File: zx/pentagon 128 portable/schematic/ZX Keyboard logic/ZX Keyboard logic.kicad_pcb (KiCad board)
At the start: 2 copper layers, 99 x 66 mm, 51 parts, among them IC1 SN74LS245DW, IC2 SN74LS27N, IC3 SN74LS245DW, J1 Conn_01x03, J2 Conn_01x14, J3 Conn_01x02

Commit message: fixed keyboard
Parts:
- removed S1: 1, SamacSys_Parts:118259104
- removed S10: 0, SamacSys_Parts:118259104
- removed S11: Q, SamacSys_Parts:118259104
- removed S12: W, SamacSys_Parts:118259104
- removed S13: E, SamacSys_Parts:118259104
- removed S14: R, SamacSys_Parts:118259104
- removed S15: T, SamacSys_Parts:118259104
- removed S16: Y, SamacSys_Parts:118259104
- removed S17: U, SamacSys_Parts:118259104
- removed S18: I, SamacSys_Parts:118259104
- removed S19: O, SamacSys_Parts:118259104
- removed S2: 2, SamacSys_Parts:118259104
- removed S20: P, SamacSys_Parts:118259104
- removed S21: A, SamacSys_Parts:118259104
- removed S22: S, SamacSys_Parts:118259104
- removed S23: D, SamacSys_Parts:118259104
- removed S24: F, SamacSys_Parts:118259104
- removed S25: G, SamacSys_Parts:118259104
- removed S26: H, SamacSys_Parts:118259104
- removed S27: J, SamacSys_Parts:118259104
- removed S28: K, SamacSys_Parts:118259104
- removed S29: L, SamacSys_Parts:118259104
- removed S3: 3, SamacSys_Parts:118259104
- removed S30: ENTER, SamacSys_Parts:118259104
- removed S31: CAPS, SamacSys_Parts:118259104
- removed S32: Z, SamacSys_Parts:118259104
- removed S33: X, SamacSys_Parts:118259104
- removed S34: C, SamacSys_Parts:118259104
- removed S35: V, SamacSys_Parts:118259104
- removed S36: B, SamacSys_Parts:118259104
- removed S37: N, SamacSys_Parts:118259104
- removed S38: M, SamacSys_Parts:118259104
- removed S39: SYMB, SamacSys_Parts:118259104
- removed S4: 4, SamacSys_Parts:118259104
- removed S40: SPACE, SamacSys_Parts:118259104
- removed S5: 5, SamacSys_Parts:118259104
- removed S6: 6, SamacSys_Parts:118259104
- removed S7: 7, SamacSys_Parts:118259104
- removed S8: 8, SamacSys_Parts:118259104
- removed S9: 9, SamacSys_Parts:118259104
- added J4: Conn_01x13, Connector_PinSocket_2.54mm:PinSocket_1x13_P2.54mm_Vertical, B.Cu at (51.8, 103.1)
- IC1: moved to B.Cu
- IC3, R1, R2, R3, R4, R?-R1: moved to F.Cu
- moved J2 34.4 mm to (50.8, 82.8), turned to 90 degrees
- moved J3 33.6 mm to (35.3, 95.2)
- moved R?-R1 23.9 mm to (79.8, 86.1)
- moved R1 21.4 mm to (78.5, 86.1)
- moved R2 18.9 mm to (77.2, 86.1)
- moved R3 16.2 mm to (75.9, 86.1)
- moved IC1 15.8 mm to (61.7, 94.5), turned to 270 degrees
- moved IC3 15.3 mm to (75.4, 94.5)
- moved R4 13.3 mm to (74.4, 86.1)
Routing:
- net /K_D0: track 204.4 -> 6.38 mm
- net /K_D1: track 173.3 -> 4.95 mm
- net /K_D2: track 152.8 -> 4.42 mm
- net /K_D3: track 135.5 -> 3.99 mm
- net /K_A15: track 131.5 -> 4.81 mm
- net /K_A14: track 122.9 -> 4.28 mm
- net /K_A13: track 114.4 -> 4.07 mm
- net /K_A8: track 114.2 -> 9.07 mm
- net /K_A9: track 108.4 -> 7.80 mm
- net /K_D4: track 102.6 -> 4.45 mm
- net /K_A10: track 103.1 -> 6.53 mm
- net /K_A12: track 62.4 -> 4.59 mm
- net /K_A11: track 60.4 -> 5.26 mm
- net +5V: track 49.7 -> 98.5 mm, vias 2 -> 0
- net /KEY_ENBL: track 29.3 -> 51.2 mm
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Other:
- board size 99 x 66 mm -> 59 x 37 mm
- board text added: "K_A10"
- board text added: "K_A11"
- board text added: "K_A12"
- board text added: "K_A13"
- board text added: "K_A14"
- board text added: "K_A15"
- board text added: "K_A8"
- board text added: "K_A9"
- board text added: "K_D0"
- board text added: "K_D1"
- board text added: "K_D2"
- board text added: "K_D3"
- board text added: "K_D4"
- board text added: "ZX Keyboard adapter"
- board text removed: "ZX Keyboard"

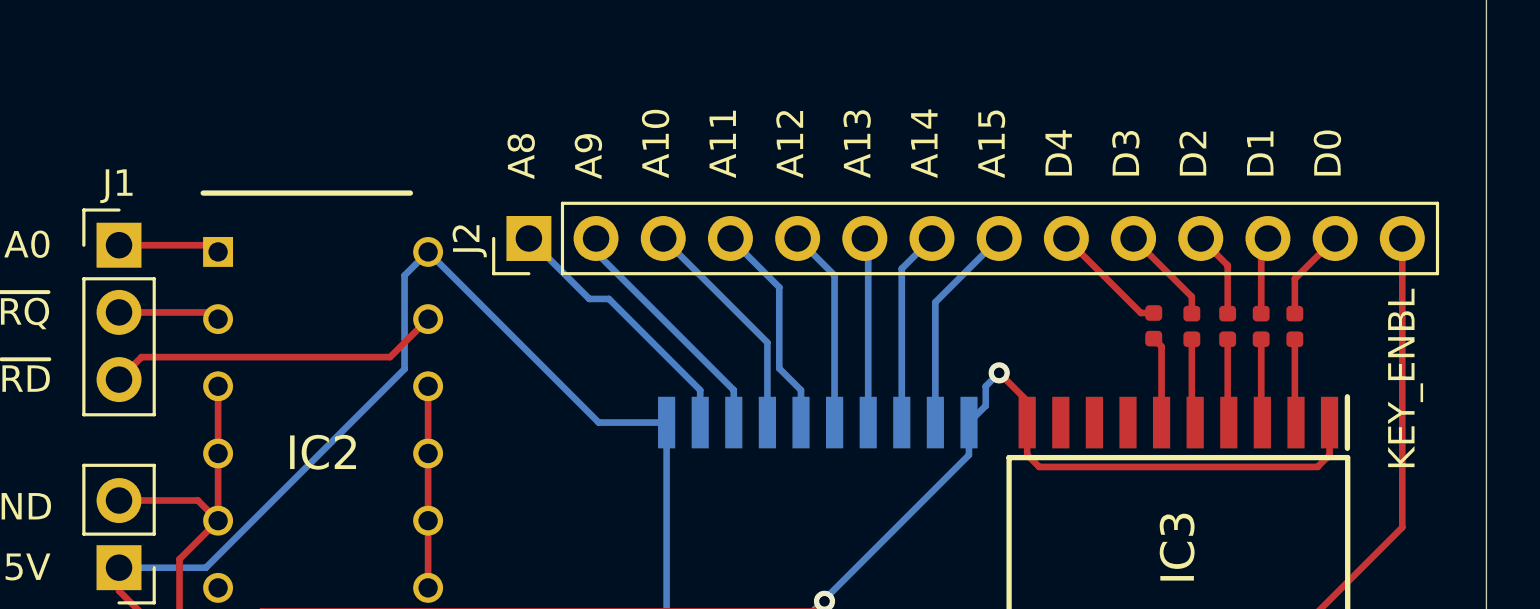
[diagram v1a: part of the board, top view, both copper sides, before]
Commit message: added z80 pdip. updated all boards
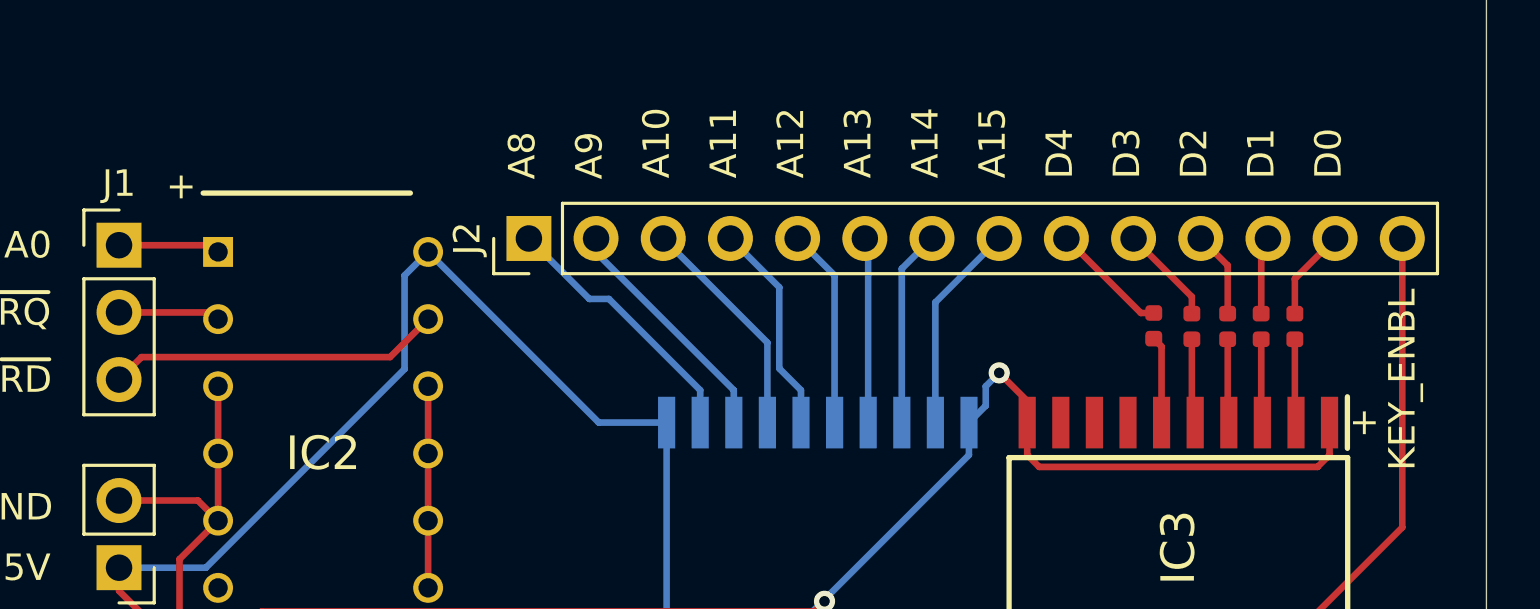
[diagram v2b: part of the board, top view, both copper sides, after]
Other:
- board text added: "+"
- board text added: "JLCJLCJLCJLC"
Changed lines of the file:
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@@
   (general
     (thickness 1.6)
-    (drawings 38)
+    (drawings 42)
     (tracks 137)
     (zones 0)
@@
       (outputformat 1)
       (mirror false)
-      (drillshape 1)
+      (drillshape 0)
       (scaleselection 1)
-      (outputdirectory ""))
+      (outputdirectory "gerber/"))
   )
   (net 0 "")
@@
       (effects (font (size 1 1) (thickness 0.15)) (justify mirror))
     )
-    (fp_text user %R (at 0 -15.24) (layer B.Fab)
-      (effects (font (size 1 1) (thickness 0.15)) (justify mirror))
-    )
     (fp_line (start -1.27 1.27) (end 0.635 1.27) (layer B.Fab) (width 0.1))
     (fp_line (start 0.635 1.27) (end 1.27 0.635) (layer B.Fab) (width 0.1))
@@
     (fp_line (start 1.75 -32.25) (end -1.8 -32.25) (layer B.CrtYd) (width 0.05))
     (fp_line (start -1.8 -32.25) (end -1.8 1.8) (layer B.CrtYd) (width 0.05))
+    (fp_text user %R (at 0 -15.24) (layer B.Fab)
+      (effects (font (size 1 1) (thickness 0.15)) (justify mirror))
+    )
     (pad 13 thru_hole oval (at 0 -30.48 270) (size 1.7 1.7) (drill 1) (layers *.Cu *.Mask)
       (net 13 /K_D0))
@@
     )
   )
+  (gr_text JLCJLCJLCJLC (at 38.4937 104.3051) (layer B.SilkS)
+    (effects (font (size 1 1) (thickness 0.15)) (justify mirror))
+  )
+  (gr_text + (at 37.6555 80.8228) (layer F.SilkS)
+    (effects (font (size 1 1) (thickness 0.15)))
+  )
+  (gr_text + (at 82.3849 89.7382) (layer F.SilkS)
+    (effects (font (size 1 1) (thickness 0.15)))
+  )
+  (gr_text + (at 54.5211 88.8873) (layer B.SilkS)
+    (effects (font (size 1 1) (thickness 0.15)) (justify mirror))
+  )
   (gr_text K_D0 (at 82.042 107.168667 90) (layer F.SilkS)
